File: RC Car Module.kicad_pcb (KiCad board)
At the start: 2 copper layers, 45 x 45 mm, 67 parts, among them J1 USB_C_Receptacle_USB2.0_14P, J2 Conn_01x13, J3 Conn_01x09, J4 Conn_01x02, J6 Conn_01x02, J7 Conn_01x02, J8 Conn_01x04, SW1 SW_Push, SW2 SW_Push, U1 AP62401WU-7, U2 W25Q16JVUXIQ TR, U3 RT6154AGQW, U4 TB6612FNG, U5 RP2040, Y1 12 MHz

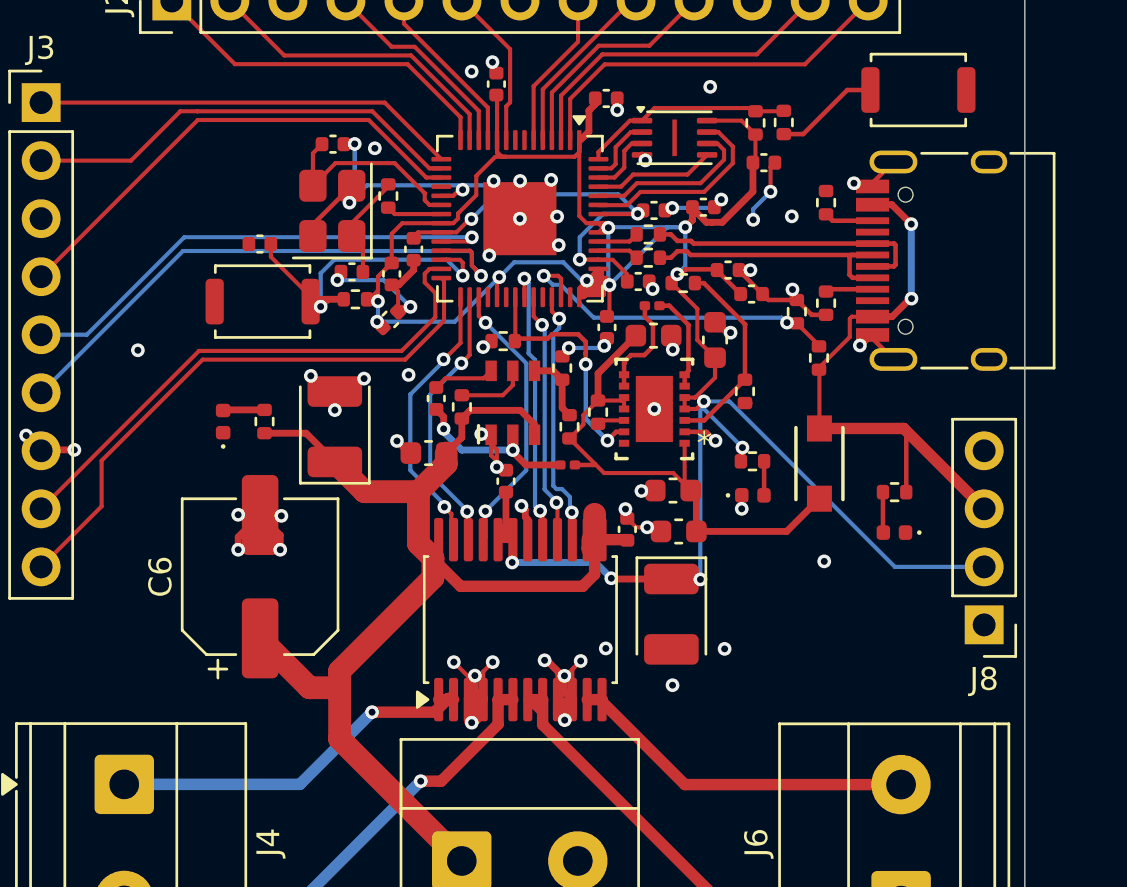
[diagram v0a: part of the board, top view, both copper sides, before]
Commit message: Began adding radio and made a couple changes to the footprints
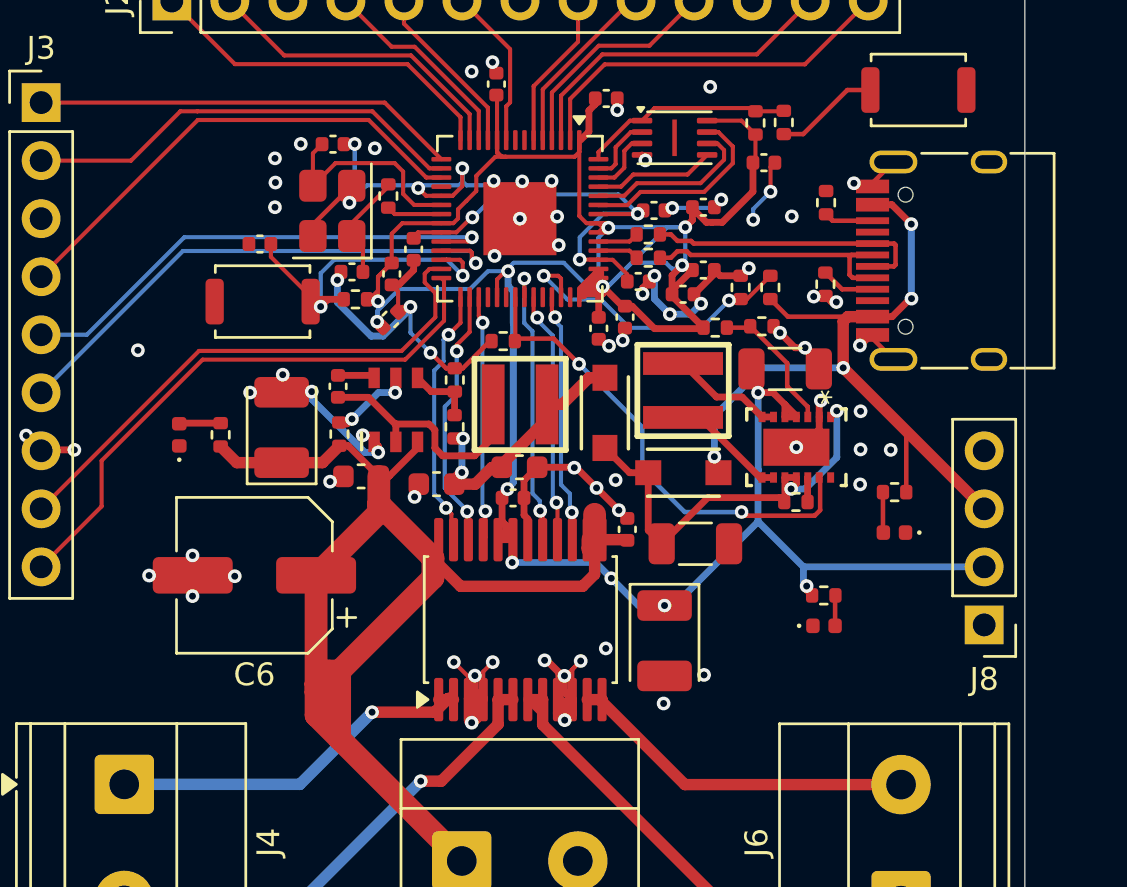
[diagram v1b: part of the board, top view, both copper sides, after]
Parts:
- added 11111: MBR120VLSFT1G, RP2040:SDO_SOD-123FL_ONS, F.Cu at (164.8, 83.4)
- added C20: 0.1uF, Capacitor_SMD:C_0402_1005Metric, F.Cu at (165.7, 79.2)
- C10, C9: footprint Capacitor_SMD:C_0603_1608Metric -> Capacitor_SMD:C_1206_3216Metric
- L1, L2: footprint Inductor_SMD:L_0201_0603Metric -> easyeda2kicad:IND-SMD_L4.0-W4.0_XAL4030-332MEC
- moved C8 10.8 mm to (157.4, 86.5)
- moved R10 9.51 mm to (173.1, 87.3), turned to 0 degrees
- moved C7 8.22 mm to (161.0, 85.8)
- moved R19 6.65 mm to (174.3, 91.4)
- moved D2 6.50 mm to (174.4, 92.8)
- moved U3 6.44 mm to (173.1, 84.9), turned to -90 degrees
- moved 1111 5.97 mm to (168.2, 86.0), turned to 0 degrees
- moved R2 5.49 mm to (153.2, 84.4)
- moved U1 5.13 mm to (155.6, 83.3)
- moved R4 5.03 mm to (158.2, 84.0)
- moved R6 4.73 mm to (158.2, 82.0)
- moved C3 4.33 mm to (153.1, 82.3)
- moved L2 3.95 mm to (168.2, 82.5), turned to 90 degrees
- moved R9 3.75 mm to (172.0, 77.9)
- moved L1 3.37 mm to (161.1, 83.1)
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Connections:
- 1111 pad 1: VSYS -> Net-(U3-VINA)
- C10 pad 1: VSYS -> Net-(U3-VINA)
- R10 pad 1: VSYS -> Net-(U3-VINA)
- U3 pad 1: VSYS -> Net-(U3-VINA)
- U3 pad 10: VSYS -> Net-(U3-VINA)
- U3 pad 11: VSYS -> Net-(U3-VINA)
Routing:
- net Net-(U3-VINA): track 0.00 -> 19.2 mm, vias 0 -> 2
- net GND: track 83.7 -> 98.4 mm, vias 66 -> 77
- net VSYS: track 24.2 -> 11.4 mm, vias 0 -> 2
- net +3V3: track 122.1 -> 134.6 mm
- net VBUS: track 25.2 -> 36.0 mm, vias 2 -> 4
- net GPIO23: track 10.9 -> 21.2 mm
- net +12V: track 53.8 -> 60.5 mm
- net Net-(U3-FB): track 8.85 -> 6.06 mm
- net Net-(U1-SW): track 8.21 -> 10.9 mm, vias 2 -> 0
- net GPIO28_ADC2: track 15.0 -> 13.4 mm
- net SWD: track 25.2 -> 23.9 mm
- net AIN1: track 12.3 -> 11.0 mm
- net Net-(U1-BST): track 2.70 -> 1.63 mm
- net PWMA: track 12.3 -> 11.4 mm
- net Net-(U1-EN): track 3.04 -> 3.68 mm, vias 0 -> 2
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
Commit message: Update ReadMe
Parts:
- added D2: LED, LED_SMD:LED_0402_1005Metric, F.Cu at (148.3, 73.5)
- added R14: 180K, Resistor_SMD:R_0402_1005Metric, F.Cu at (173.9, 79.9)
- added R20: 330, Resistor_SMD:R_0402_1005Metric, F.Cu at (148.3, 72.0)
- C4: renamed from C5; footprint Capacitor_SMD:C_0603_1608Metric -> Capacitor_Tantalum_SMD:CP_EIA-3528-15_AVX-H
- R12: value 180K -> 680K
- R8: value 1M -> 330K
- moved C14 3.21 mm to (146.6, 92.1)
- moved C4 2.69 mm to (153.2, 88.7)
- moved R12 0.11 mm to (171.7, 79.7)
- renumbered 1111 to 111111, 11111 to 1111111, C3 to C1, C11 to C10, C27 to C11, C6 to C14, C14 to C15, C15 to C16, C16 to C17, C17 to C18, C18 to C19, C1 to C2, C19 to C20, C20 to C21, C21 to C22, C22 to C23, C23 to C24, C24 to C25, C25 to C26, C26 to C27, C2 to C3, C4 to C5, C7 to C6, C8 to C7, C9 to C8, C10 to C9, D2 to D1, J6 to J5, J8 to J6, R2 to R1, R14 to R15, R15 to R16, R16 to R17, R17 to R18, R4 to R2, R20 to R21, R21 to R22, R1 to R3, R3 to R4
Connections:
- R12 pad 1: Net-(U3-FB) -> Net-(R12-Pad1)
- R12 pad 2: GND -> Net-(U3-FB)
- R8 pad 2: Net-(U3-FB) -> Net-(R12-Pad1)
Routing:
- net GND: track 98.4 -> 106.7 mm, vias 77 -> 79
- net GPIO14: track 21.4 -> 23.1 mm
- net Net-(D2-A): track 0.00 -> 1.50 mm
- net Net-(R12-Pad1): track 0.00 -> 1.04 mm
- net +12V: track 60.5 -> 61.5 mm

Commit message: Update Readme
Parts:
- removed the C15 at (156.4, 76.3)
- removed the C23 at (155.4, 79.3)
- removed the C24 at (155.4, 77.3)
- removed C27: 0.1uF, Capacitor_SMD:C_0402_1005Metric
- removed the R12 at (171.7, 79.7)
- removed the R15 at (160.3, 80.3)
- removed the R16 at (153.8, 78.5)
- removed SW2: SW_Push, Button_Switch_SMD:SW_Push_SPST_NO_Alps_SKRK
- added C10: 1uF, Capacitor_SMD:C_0402_1005Metric, F.Cu at (55.1, 33.5)
- added C14: 0.1uF, Capacitor_SMD:C_0402_1005Metric, F.Cu at (49.4, 35.5)
- added R7: 100K, Resistor_SMD:R_0402_1005Metric, F.Cu at (61.6, 42.6)
- added TP1: TestPoint, TestPoint:TestPoint_Pad_1.0x1.0mm, B.Cu at (38.0, 40.6)
- added TP2: TestPoint, TestPoint:TestPoint_Pad_1.0x1.0mm, B.Cu at (53.7, 39.3)
- added TP3: TestPoint, TestPoint:TestPoint_Pad_1.0x1.0mm, B.Cu at (60.8, 42.7)
- C4: footprint Capacitor_Tantalum_SMD:CP_EIA-3528-15_AVX-H -> Capacitor_SMD:C_1206_3216Metric
- C6, C7: footprint Capacitor_SMD:C_0603_1608Metric -> Capacitor_SMD:C_1206_3216Metric
- C8: renamed from C9; value 47uF -> 10uF
- C9: renamed from C8; value 47uF -> 22uF
- D1, D2, D3, D4: footprint LED_SMD:LED_0402_1005Metric -> LED_SMD:LED_0805_2012Metric
- L2: footprint easyeda2kicad:IND-SMD_L4.0-W4.0_XAL4030-332MEC -> Inductor_SMD:L_1008_2520Metric
- R9: renamed from R8; value 330K -> 1.02M
- U3: value RT6154AGQW -> RT6150BGQW; footprint RP2040:QFN_4AGQW_RIT -> easyeda2kicad:WSON-10_L2.5-W2.5-P0.50-BL-EP
- moved C19 133.4 mm to (43.4, 31.2), turned to 180 degrees
- moved C11 130.9 mm to (43.4, 32.5), turned to 180 degrees
- moved C4 126.0 mm to (37.0, 39.9), turned to 90 degrees
- moved C6 123.7 mm to (47.2, 37.3), turned to 180 degrees
- moved R6 123.7 mm to (43.3, 36.3), turned to 180 degrees
- moved R2 123.2 mm to (44.0, 37.8)
- moved C13 122.1 mm to (54.5, 35.2), turned to -90 degrees
- moved U1 122.0 mm to (41.9, 39.2)
- moved R1 122.0 mm to (39.4, 40.2)
- moved C1 122.0 mm to (39.4, 38.0)
- moved L1 122.0 mm to (46.6, 41.0)
- moved C5 121.9 mm to (39.8, 33.7)
- moved C2 121.9 mm to (39.2, 27.7)
- moved 1111111111111 121.5 mm to (57.0, 37.0)
- moved Y1 121.4 mm to (39.6, 30.6)
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- renumbered 111111 to 1111111111111, 1111111 to 11111111111111, C16 to C11, C17 to C12, C18 to C13, C20 to C15, C21 to C16, C22 to C17, C25 to C20, C26 to C21, C10 to C22, C11 to C23, C12 to C24, C13 to C25, C14 to C26, J4 to J3, J5 to J4, J3 to J5, J7 to J6, J6 to J7, R9 to R10, R14 to R12, R10 to R13, R13 to R14, R17 to R15, R18 to R16, R19 to R17, R20 to R18, R21 to R19, R22 to R20, R7 to R8
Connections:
- 1111111111111 pad 1: Net-(U3-VINA) -> Net-(U3-VIN)
- 11111111111111 pad 1: Net-(U3-VINA) -> Net-(U3-VIN)
- C8 pad 1: Net-(U3-VINA) -> Net-(U3-VIN)
- J2 pad 6: GPIO7 -> GPIO6
- L2 pad 1: Net-(L2-Pad1) -> Net-(U3-LX1)
- L2 pad 2: Net-(L2-Pad2) -> Net-(U3-LX2)
- R13 pad 1: Net-(U3-VINA) -> Net-(U3-PS)
- R13 pad 2: 3V3_EN -> GND
- R9 pad 2: Net-(R12-Pad1) -> Net-(U3-FB)
- U3 pad 1: Net-(U3-VINA) -> +3V3
- U3 pad 10: Net-(U3-VINA) -> Net-(U3-FB)
- U3 pad 11: Net-(U3-VINA) -> GND
- U3 pad 2: GND -> Net-(U3-LX2)
- U3 pad 3: Net-(U3-FB) -> GND
- U3 pad 4: +3V3 -> Net-(U3-LX1)
- U3 pad 5: +3V3 -> Net-(U3-VIN)
- U3 pad 6: Net-(L2-Pad2) -> Net-(U3-EN)
- U3 pad 7: Net-(L2-Pad2) -> Net-(U3-PS)
- U3 pad 8: Net-(L2-Pad1) -> Net-(U3-VIN)
- U3 pad 9: Net-(L2-Pad1) -> GND
- U4 pad 19: +3V3 -> STBY
- U5 pad 26: Net-(U5-RUN) -> unconnected-(U5-RUN-Pad26)
- U5 pad 34: unconnected-(U5-GPIO22-Pad34) -> STBY
- U5 pad 35: GPIO23 -> unconnected-(U5-GPIO23-Pad35)
- U5 pad 8: unconnected-(U5-GPIO6-Pad8) -> GPIO6
- U5 pad 9: GPIO7 -> unconnected-(U5-GPIO7-Pad9)
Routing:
- net +12V: track 61.5 -> 94.2 mm, vias 0 -> 1
- net VSYS: track 11.4 -> 38.2 mm, vias 2 -> 1
- net Net-(U3-VIN): track 0.00 -> 26.2 mm, vias 0 -> 2
- net GND: track 106.7 -> 132.2 mm, vias 79 -> 128
- net +3V3: track 134.6 -> 113.2 mm, vias 13 -> 10
- net GPIO23: track 21.2 -> 0.00 mm, vias 2 -> 0
- net Net-(U3-VINA): track 19.2 -> 0.00 mm, vias 2 -> 0
- net Net-(U5-RUN): track 16.0 -> 0.00 mm, vias 2 -> 0
- net STBY: track 0.00 -> 15.2 mm, vias 0 -> 2
- net GPIO6: track 0.00 -> 7.05 mm
- net GPIO7: track 7.03 -> 0.00 mm
- net VBUS: track 36.0 -> 30.1 mm, vias 4 -> 5
- net Net-(L2-Pad1): track 5.05 -> 0.00 mm
- net Net-(L2-Pad2): track 4.93 -> 0.00 mm
- net Net-(U3-FB): track 6.54 -> 2.69 mm
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- added copper zone on F.Cu, net +12V
